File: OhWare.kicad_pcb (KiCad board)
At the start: 2 copper layers, 39.7 x 39.5 mm, 0 parts

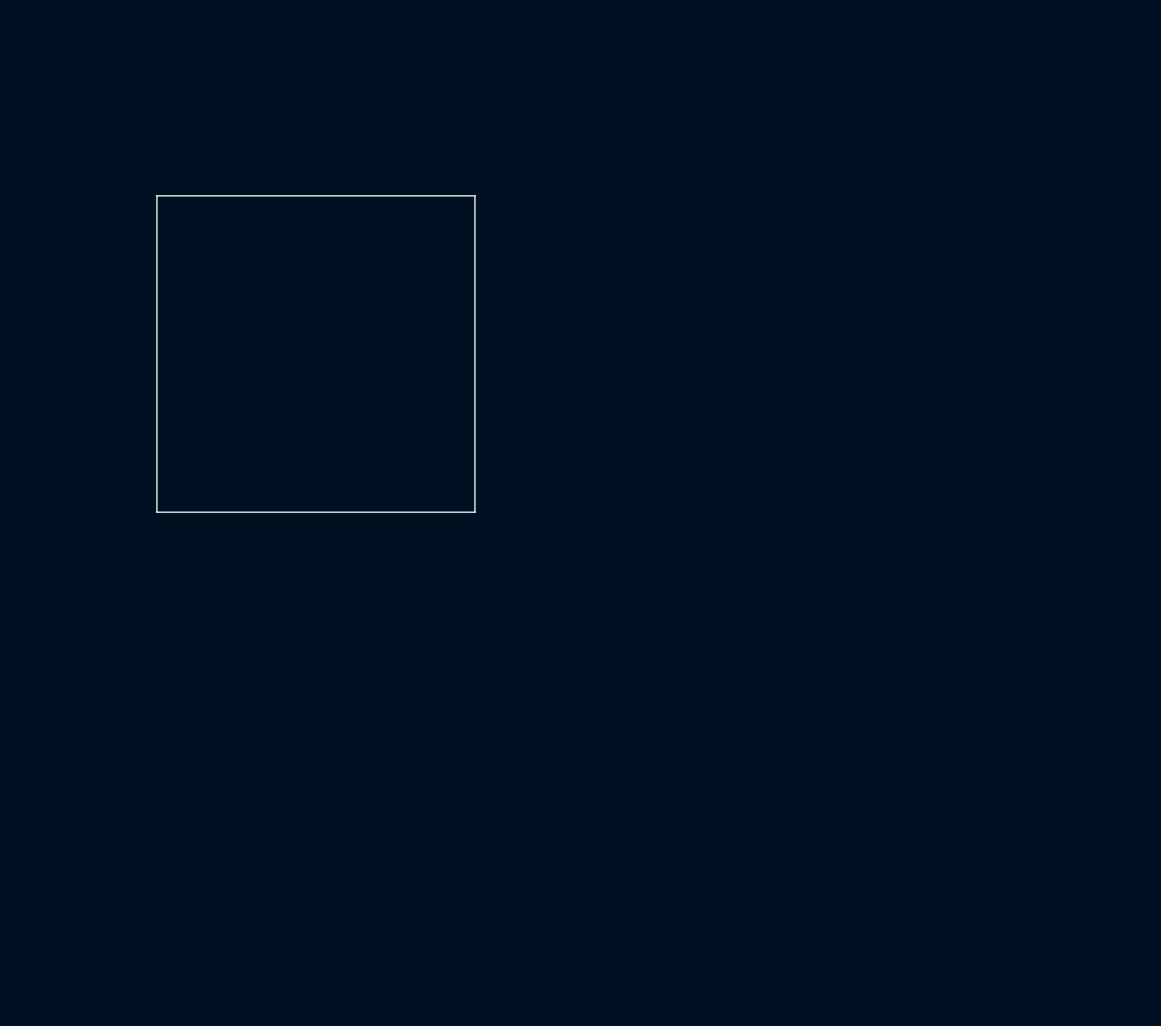
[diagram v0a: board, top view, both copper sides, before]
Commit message: Schematic--Footprint link
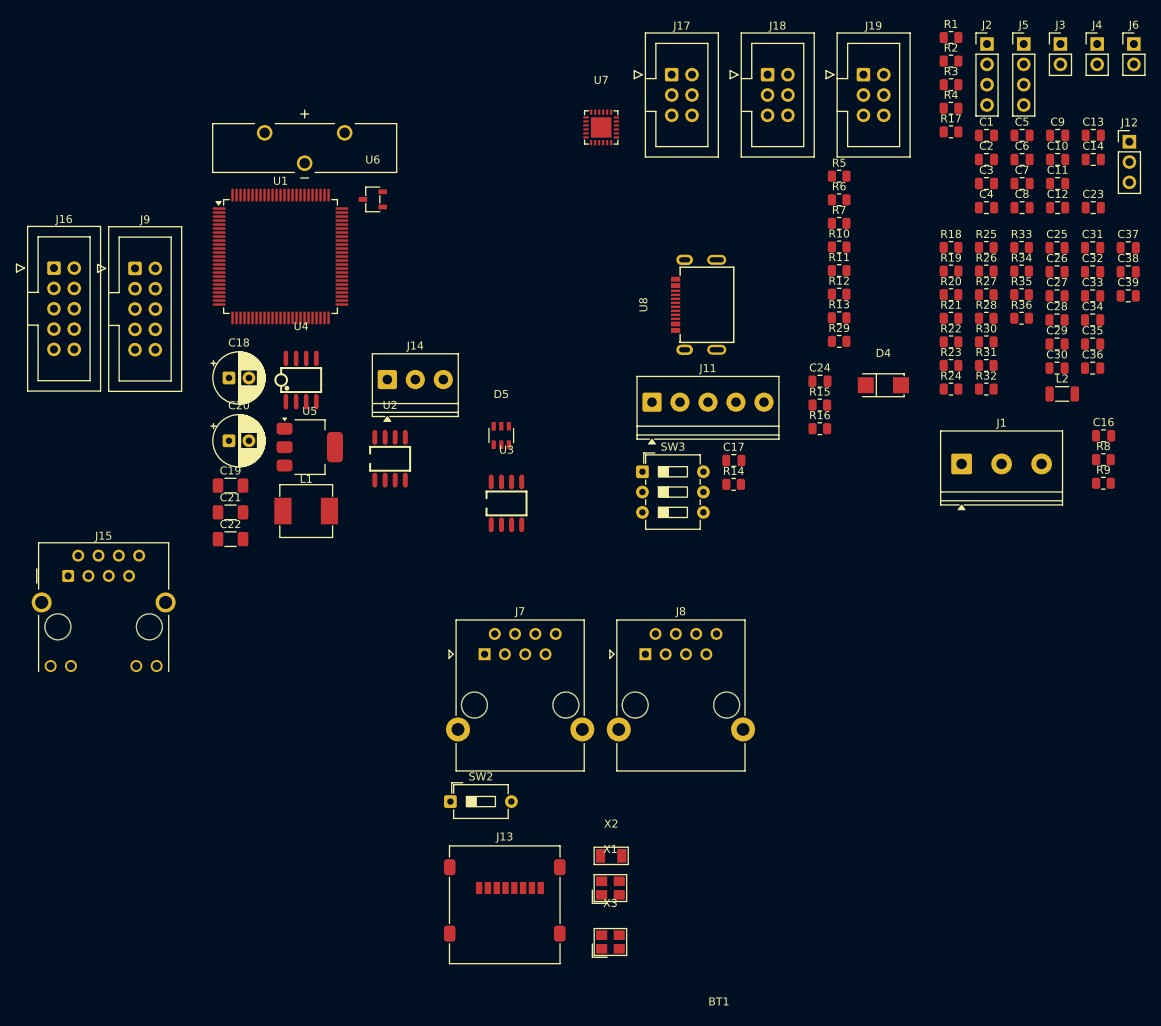
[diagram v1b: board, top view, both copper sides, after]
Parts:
- added BT1: CR2032, EasyEDA:BAT_1074, F.Cu at (111.2, 81.0)
- added C1: 20p, Capacitor_SMD:C_0805_2012Metric, F.Cu at (196.4, 79.5)
- added C10: 100n, Capacitor_SMD:C_0805_2012Metric, F.Cu at (205.3, 82.5)
- added C11: 100n, Capacitor_SMD:C_0805_2012Metric, F.Cu at (205.3, 85.5)
- added C12: 100n, Capacitor_SMD:C_0805_2012Metric, F.Cu at (205.3, 88.5)
- added C13: 100n, Capacitor_SMD:C_0805_2012Metric, F.Cu at (209.7, 79.5)
- added C14: 4.7u, Capacitor_SMD:C_0805_2012Metric, F.Cu at (209.7, 82.5)
- added C16: 100n, Capacitor_SMD:C_0805_2012Metric, F.Cu at (211.0, 117.0)
- added C17: 0.1u, Capacitor_SMD:C_0805_2012Metric, F.Cu at (164.8, 120.1)
- added C18: 100uF-35V, Capacitor_THT:CP_Radial_D6.3mm_P2.50mm, F.Cu at (101.7, 109.8)
- added C19: 1u-50V, Capacitor_SMD:C_1206_3216Metric_Pad1.33x1.80mm_HandSolder, F.Cu at (101.9, 123.2)
- added C2: 20p, Capacitor_SMD:C_0805_2012Metric, F.Cu at (196.4, 82.5)
- added C20: 180uF-10V, Capacitor_THT:CP_Radial_D6.3mm_P2.50mm, F.Cu at (101.7, 117.6)
- added C21: 10u, Capacitor_SMD:C_1206_3216Metric_Pad1.33x1.80mm_HandSolder, F.Cu at (101.9, 126.6)
- added C22: 10u, Capacitor_SMD:C_1206_3216Metric_Pad1.33x1.80mm_HandSolder, F.Cu at (101.9, 129.9)
- added C23: 100n, Capacitor_SMD:C_0805_2012Metric, F.Cu at (209.7, 88.5)
- added C24: 100n, Capacitor_SMD:C_0805_2012Metric, F.Cu at (175.6, 110.2)
- added C25: 10pF, Capacitor_SMD:C_0805_2012Metric, F.Cu at (205.2, 93.5)
- added C26: 10pF, Capacitor_SMD:C_0805_2012Metric, F.Cu at (205.2, 96.5)
- added C27: 10pF, Capacitor_SMD:C_0805_2012Metric, F.Cu at (205.2, 99.5)
- added C28: 10pF, Capacitor_SMD:C_0805_2012Metric, F.Cu at (205.2, 102.5)
- added C29: 22nF, Capacitor_SMD:C_0805_2012Metric, F.Cu at (205.2, 105.5)
- added C3: 2.2u, Capacitor_SMD:C_0805_2012Metric, F.Cu at (196.4, 85.5)
- added C30: 0.1uF, Capacitor_SMD:C_0805_2012Metric, F.Cu at (205.2, 108.6)
- added C31: 4.7u, Capacitor_SMD:C_0805_2012Metric, F.Cu at (209.7, 93.5)
- added C32: 4.7u, Capacitor_SMD:C_0805_2012Metric, F.Cu at (209.7, 96.5)
- added C33: 0.1uF, Capacitor_SMD:C_0805_2012Metric, F.Cu at (209.7, 99.5)
- added C34: 0.1uF, Capacitor_SMD:C_0805_2012Metric, F.Cu at (209.7, 102.5)
- added C35: 0.1uF, Capacitor_SMD:C_0805_2012Metric, F.Cu at (209.7, 105.5)
- added C36: 1uF, Capacitor_SMD:C_0805_2012Metric, F.Cu at (209.7, 108.6)
- added C37: 0.1uF, Capacitor_SMD:C_0805_2012Metric, F.Cu at (214.1, 93.5)
- added C38: 30pF, Capacitor_SMD:C_0805_2012Metric, F.Cu at (214.1, 96.5)
- added C39: 30pF, Capacitor_SMD:C_0805_2012Metric, F.Cu at (214.1, 99.5)
- added C4: 2.2u, Capacitor_SMD:C_0805_2012Metric, F.Cu at (196.4, 88.5)
- added C5: 12.5pF, Capacitor_SMD:C_0805_2012Metric, F.Cu at (200.8, 79.5)
- added C6: 12.5pF, Capacitor_SMD:C_0805_2012Metric, F.Cu at (200.8, 82.5)
- added C7: 100n, Capacitor_SMD:C_0805_2012Metric, F.Cu at (200.8, 85.5)
- added C8: 100n, Capacitor_SMD:C_0805_2012Metric, F.Cu at (200.8, 88.5)
- added C9: 100n, Capacitor_SMD:C_0805_2012Metric, F.Cu at (205.3, 79.5)
- added D4: SS34_C8678, EasyEDA:SMA_L4.3-W2.6-LS5.2-RD, F.Cu at (183.5, 110.7)
- added D5: USBLC6-2SC6, EasyEDA:SOT-23-6_L2.9-W1.6-P0.95-LS2.8-BL, F.Cu at (135.7, 117.0)
- added J1: Screw_Terminal_01x03, TerminalBlock_Phoenix:TerminalBlock_Phoenix_PT-1,5-3-5.0-H_1x03_P5.00mm_Horizontal, F.Cu at (193.3, 120.5)
- added J11: Screw_Terminal_01x05, TerminalBlock_Phoenix:TerminalBlock_Phoenix_PT-1,5-5-3.5-H_1x05_P3.50mm_Horizontal, F.Cu at (154.6, 112.8)
- added J12: Conn_01x03_Pin, Connector_PinHeader_2.54mm:PinHeader_1x03_P2.54mm_Vertical, F.Cu at (214.3, 80.3)
- added J13: Micro_SD_Card, Connector_Card:microSD_HC_Molex_47219-2001, F.Cu at (136.2, 175.6)
- added J14: Screw_Terminal_01x03, TerminalBlock_Phoenix:TerminalBlock_Phoenix_PT-1,5-3-3.5-H_1x03_P3.50mm_Horizontal, F.Cu at (121.5, 110.0)
- added J15: RJ45_Hanrun_HR911105A_Horizontal, Connector_RJ:RJ45_Hanrun_HR911105A_Horizontal, F.Cu at (81.6, 134.5)
- added J16: Conn_02x05_Odd_Even, Connector_IDC:IDC-Header_2x05_P2.54mm_Vertical, F.Cu at (79.8, 96.1)
- added J17: Conn_02x03_Odd_Even, Connector_IDC:IDC-Header_2x03_P2.54mm_Vertical, F.Cu at (157.0, 71.9)
- added J18: Conn_02x03_Odd_Even, Connector_IDC:IDC-Header_2x03_P2.54mm_Vertical, F.Cu at (169.0, 71.9)
- added J19: Conn_02x03_Odd_Even, Connector_IDC:IDC-Header_2x03_P2.54mm_Vertical, F.Cu at (181.0, 71.9)
- added J2: Conn_01x04_Pin, Connector_PinHeader_2.54mm:PinHeader_1x04_P2.54mm_Vertical, F.Cu at (196.5, 68.0)
- added J3: Conn_01x02_Pin, Connector_PinHeader_2.54mm:PinHeader_1x02_P2.54mm_Vertical, F.Cu at (205.6, 68.0)
- added J4: Conn_01x02_Pin, Connector_PinHeader_2.54mm:PinHeader_1x02_P2.54mm_Vertical, F.Cu at (210.2, 68.0)
- added J5: Conn_01x04_Pin, Connector_PinHeader_2.54mm:PinHeader_1x04_P2.54mm_Vertical, F.Cu at (201.1, 68.0)
- added J6: Conn_01x02_Pin, Connector_PinHeader_2.54mm:PinHeader_1x02_P2.54mm_Vertical, F.Cu at (214.8, 68.0)
- added J7: 8P8C_Shielded, Connector_RJ:RJ45_Ninigi_GE, F.Cu at (133.7, 144.3)
- added J8: 8P8C_Shielded, Connector_RJ:RJ45_Ninigi_GE, F.Cu at (153.8, 144.3)
- added J9: Conn_02x05_Odd_Even, Connector_IDC:IDC-Header_2x05_P2.54mm_Vertical, F.Cu at (90.0, 96.1)
- added L1: SMMS0650-680M, EasyEDA:IND-SMD_L7.1-W6.6_H5.0, F.Cu at (111.4, 126.4)
- added L2: 2A/0.05, Inductor_SMD:L_1206_3216Metric, F.Cu at (205.9, 111.8)
- added R1: 10K, Resistor_SMD:R_0805_2012Metric, F.Cu at (192.0, 67.2)
- added R10: 0, Resistor_SMD:R_0805_2012Metric, F.Cu at (178.0, 93.4)
- added R11: 0, Resistor_SMD:R_0805_2012Metric, F.Cu at (178.0, 96.4)
- added R12: 0, Resistor_SMD:R_0805_2012Metric, F.Cu at (178.0, 99.3)
- added R13: 0, Resistor_SMD:R_0805_2012Metric, F.Cu at (178.0, 102.3)
- added R14: 120, Resistor_SMD:R_0805_2012Metric, F.Cu at (164.8, 123.1)
- added R15: 0, Resistor_SMD:R_0805_2012Metric, F.Cu at (175.6, 113.2)
- added R16: 0, Resistor_SMD:R_0805_2012Metric, F.Cu at (175.6, 116.1)
- added R17: 1k, Resistor_SMD:R_0805_2012Metric, F.Cu at (192.0, 79.0)
- added R18: 1.5k-1%, Resistor_SMD:R_0805_2012Metric, F.Cu at (192.0, 93.5)
- added R19: 1M, Resistor_SMD:R_0805_2012Metric, F.Cu at (192.0, 96.4)
- added R2: 10K, Resistor_SMD:R_0805_2012Metric, F.Cu at (192.0, 70.2)
- added R20: 0, Resistor_SMD:R_0805_2012Metric, F.Cu at (192.0, 99.4)
- added R21: 49.9-1%, Resistor_SMD:R_0805_2012Metric, F.Cu at (192.0, 102.3)
- added R22: 49.9-1%, Resistor_SMD:R_0805_2012Metric, F.Cu at (192.0, 105.3)
- added R23: 49.9-1%, Resistor_SMD:R_0805_2012Metric, F.Cu at (192.0, 108.2)
- added R24: 49.9-1%, Resistor_SMD:R_0805_2012Metric, F.Cu at (192.0, 111.2)
- added R25: 12.1k-1%, Resistor_SMD:R_0805_2012Metric, F.Cu at (196.4, 93.5)
- added R26: 33, Resistor_SMD:R_0805_2012Metric, F.Cu at (196.4, 96.4)
- added R27: 10, Resistor_SMD:R_0805_2012Metric, F.Cu at (196.4, 99.4)
- added R28: 10, Resistor_SMD:R_0805_2012Metric, F.Cu at (196.4, 102.3)
- added R29: 0, Resistor_SMD:R_0805_2012Metric, F.Cu at (178.0, 105.2)
- added R3: 10K, Resistor_SMD:R_0805_2012Metric, F.Cu at (192.0, 73.1)
- added R30: 10, Resistor_SMD:R_0805_2012Metric, F.Cu at (196.4, 105.3)
- added R31: 4.7k, Resistor_SMD:R_0805_2012Metric, F.Cu at (196.4, 108.2)
- added R32: 4.7k, Resistor_SMD:R_0805_2012Metric, F.Cu at (196.4, 111.2)
- added R33: 4.7k, Resistor_SMD:R_0805_2012Metric, F.Cu at (200.8, 93.5)
- added R34: 10k, Resistor_SMD:R_0805_2012Metric, F.Cu at (200.8, 96.4)
- added R35: 470, Resistor_SMD:R_0805_2012Metric, F.Cu at (200.8, 99.4)
- added R36: 470, Resistor_SMD:R_0805_2012Metric, F.Cu at (200.8, 102.3)
- added R4: 10K, Resistor_SMD:R_0805_2012Metric, F.Cu at (192.0, 76.1)
- added R5: 0, Resistor_SMD:R_0805_2012Metric, F.Cu at (178.0, 84.6)
- added R6: 0, Resistor_SMD:R_0805_2012Metric, F.Cu at (178.0, 87.5)
- added R7: 0, Resistor_SMD:R_0805_2012Metric, F.Cu at (178.0, 90.5)
- added R8: 10k, Resistor_SMD:R_0805_2012Metric, F.Cu at (211.0, 120.0)
- added R9: 120, Resistor_SMD:R_0805_2012Metric, F.Cu at (211.0, 123.0)
- added SW2: SW_DIP_x01, Button_Switch_THT:SW_DIP_SPSTx01_Slide_6.7x4.1mm_W7.62mm_P2.54mm_LowProfile, F.Cu at (129.4, 162.7)
- added SW3: SW_DIP_x03, Button_Switch_THT:SW_DIP_SPSTx03_Slide_6.7x9.18mm_W7.62mm_P2.54mm_LowProfile, F.Cu at (153.4, 121.5)
- added U1: STM32F407VETx, Package_QFP:LQFP-100_14x14mm_P0.5mm, F.Cu at (108.2, 94.6)
- added U2: SIT65HVD230DR, EasyEDA:SOP-8_L4.9-W3.9-P1.27-LS6.0-BL, F.Cu at (121.8, 119.9)
- added U3: SIT3490EESA, EasyEDA:SOP-8_L4.9-W3.9-P1.27-LS6.0-BL, F.Cu at (136.4, 125.5)
- added U4: XL1509-5.0E1, EasyEDA:SOIC-8_L5.0-W4.0-P1.27-LS6.0-BL, F.Cu at (110.7, 110.0)
- added U5: AMS1117-3.3, Package_TO_SOT_SMD:SOT-223-3_TabPin2, F.Cu at (111.8, 118.4)
- added U6: TL431M-0.3%-6AF, EasyEDA:SOT-23-3_L2.9-W1.6-P1.90-LS2.8-BR, F.Cu at (119.7, 87.5)
- added U7: LAN8720AI-CP-TR, EasyEDA:QFN-24_L4.0-W4.0-P0.50-BL-EP2.6, F.Cu at (148.2, 78.5)
- added U8: USB-TYPE-C-016, EasyEDA:USB-SMD_TYPE-C16PCB1.6073, F.Cu at (160.1, 100.6)
- added X1: X32258MOB4SI, EasyEDA:CRYSTAL-SMD_4P-L3.2-W2.5-BL, F.Cu at (149.4, 173.6)
- added X2: ABS07-32.768KHZ-T, EasyEDA:OSC-SMD_2P-L3.2-W1.5, F.Cu at (149.5, 169.5)
- added X3: XL2EL89CSI-111YLC-25M, EasyEDA:CRYSTAL-SMD_4P-L3.2-W2.5-BL, F.Cu at (149.4, 180.3)
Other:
- board outline removed
